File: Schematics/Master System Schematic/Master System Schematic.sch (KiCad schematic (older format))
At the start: 35 parts, among them J1 GND, J2 TS+, J3 TS-, SW1 GLVMS, SW10 SMD, SW11 BRAKE_SWITCH, SW12 SW_SPST_Pressure, SW13 SW_SPST_Pressure, SW2 SideMounted (BRB), SW3 SideMounted (BRB), SW4 Brake Over-Travel Switch, SW5 Latching Circuit Reset [Momen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, SW6 Cockpit Shutdown (BRB), SW7 TSMS, SW8 SMD, SW9 HVD, U3 FuseBox_PSZACCEPS052H, U4 Bender_Isometer_IR155-3204, U6 RinehartPM100DX_MotorControll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, U7 Emrax228HV_Motor

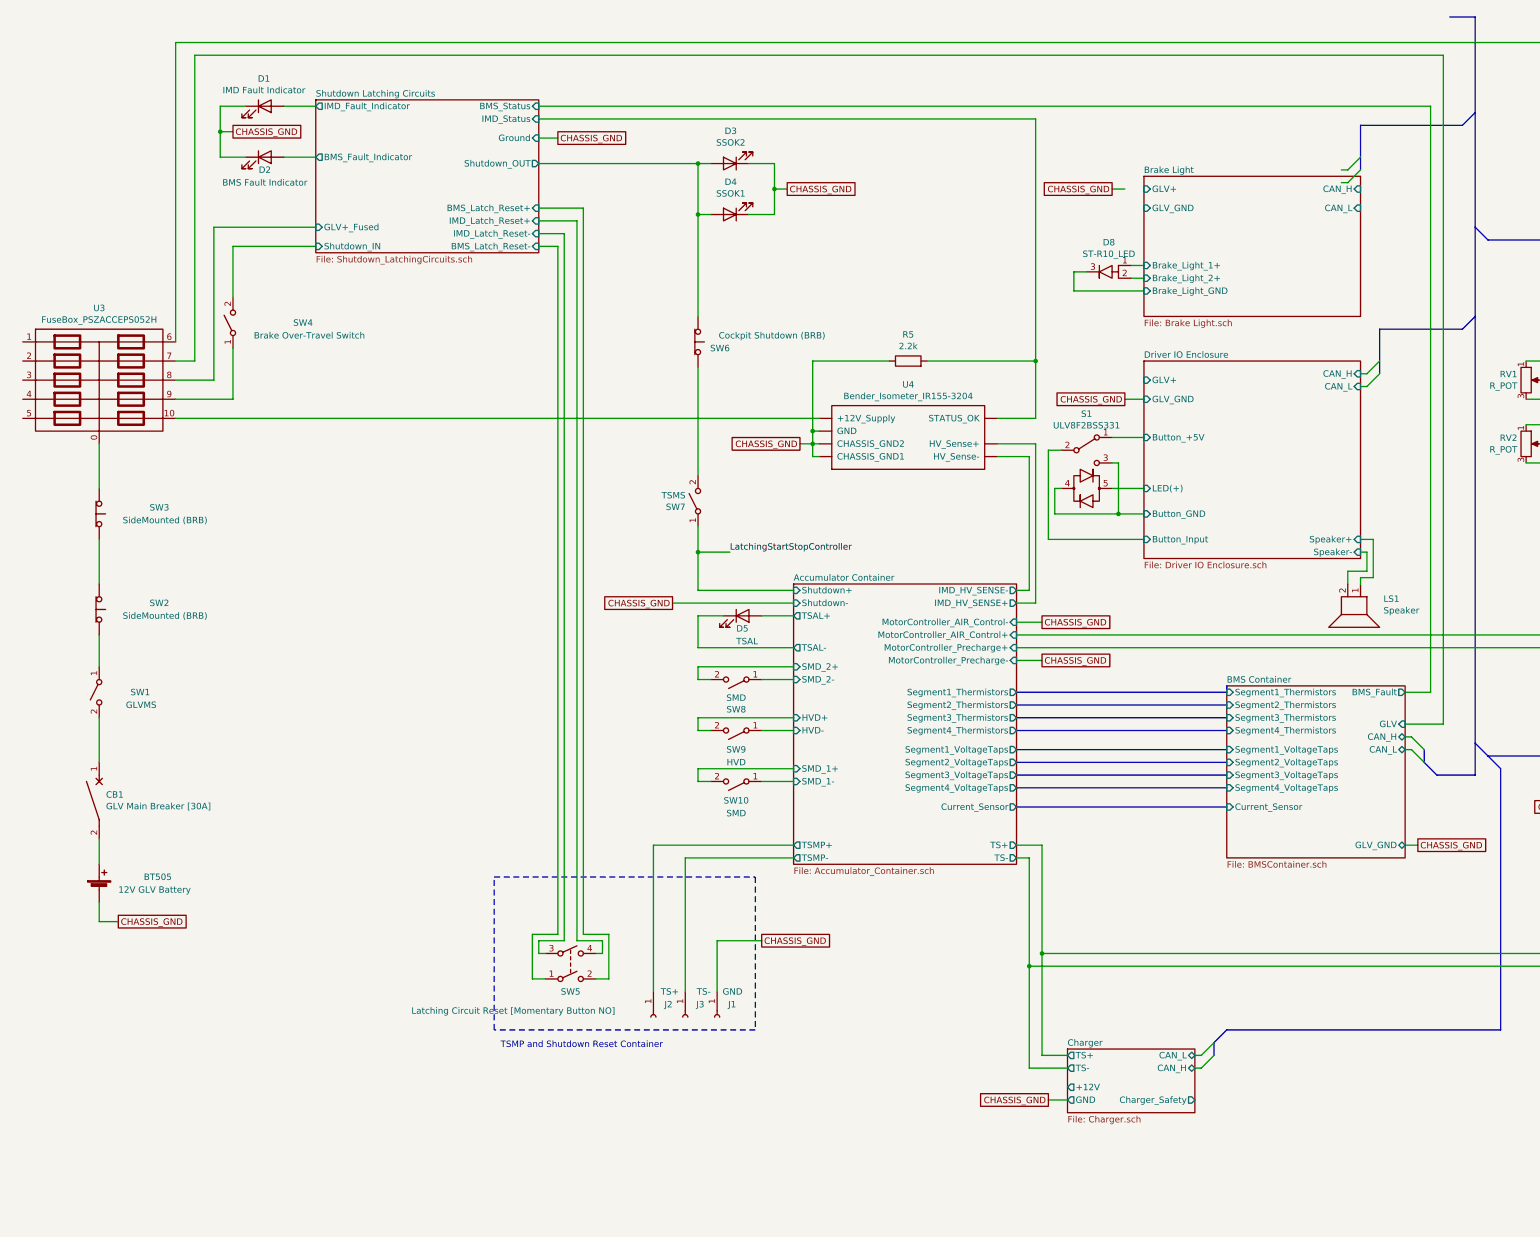
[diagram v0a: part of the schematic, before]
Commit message: Cooling Pump, TSMP container Updates
>Added Cooling pump relay
>Added Cooling pump
>Added +12V plug to TSMP container
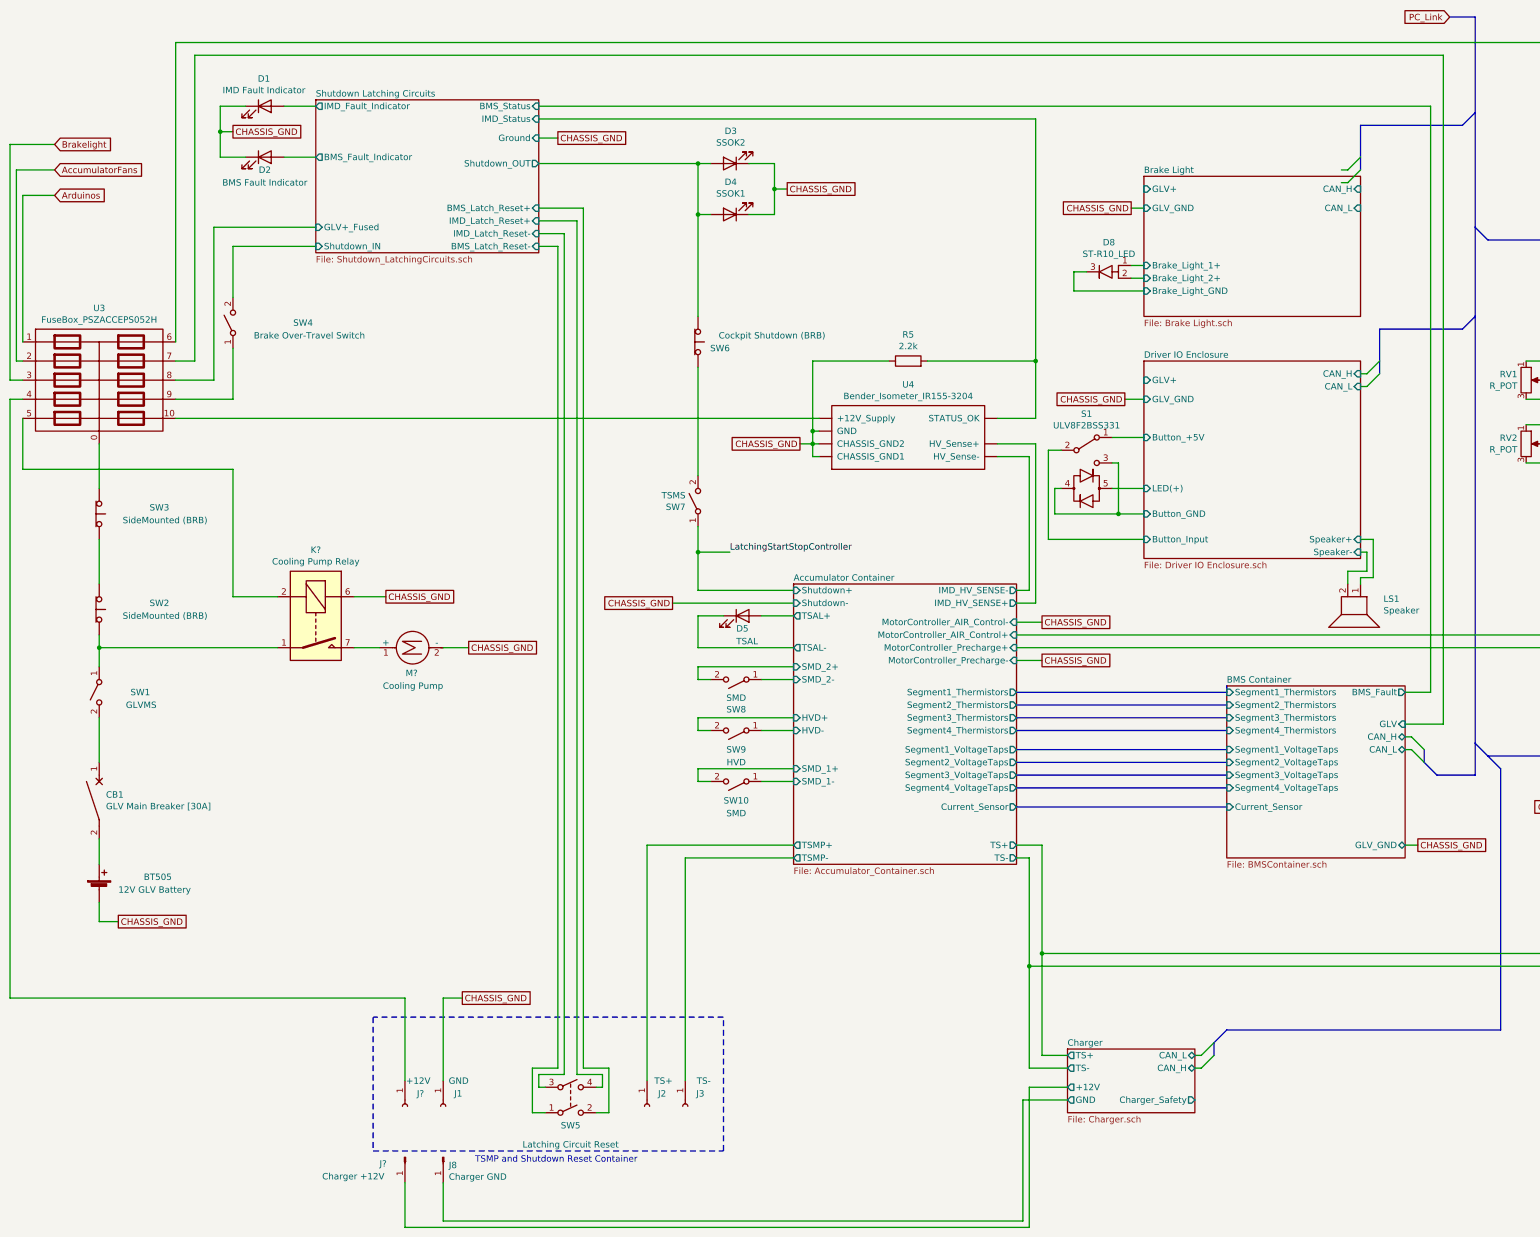
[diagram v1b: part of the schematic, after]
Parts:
- added J8: Charger GND, symbol Connector:Conn_01x01_Male
- added J?: Charger +12V, symbol Connector:Conn_01x01_Male
- added J?: +12V, symbol Connector:Conn_01x01_Female
- added K?: Cooling Pump Relay, Relay_THT:Relay_StandexMeder_DIP_LowProfile, symbol Master-System-Schematic-cache:Relay_DIPxx-1Axx-11x
- added M?: Cooling Pump, symbol Motor:Motor_DC
- SW5: value Latching Circuit Reset [Momentary Button NO] -> Latching Circuit Reset
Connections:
- net CHASSIS_GND: now also K?.6, M?.2 (-)
- net Charger/+12V: now also J?.1 (Pin_1)
- net at SW1.1 (A), SW2.2 (B): now also K?.1, K?.14
- net Arduinos: now reaches U3.1
- net AccumulatorFans: now reaches U3.2
- net Brakelight: now reaches U3.3
- net at U3.4: now also J?.1 (Pin_1)
- net at U3.5: now also K?.2
- new net: U3.6, U6.23 (CANB_H), U6.8 (Reverse_Enable_Switch)
- new net: U6.~ (TS-), U7.~ (AC3) (x2)
- new net: K?.7, K?.8, M?.1 (+)
- new net Charger/GND: J8.1 (Pin_1)
- now unconnected: U6.23 (CANB_H), U6.8 (Reverse_Enable_Switch)
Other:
- moved on the sheet: J1, J2, J3, SW5
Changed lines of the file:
@@
 EESchema Schematic File Version 4
-LIBS:Master System Schematic-cache
 EELAYER 30 0
 EELAYER END
@@
 	1250 6300 1250 6650
 Wire Wire Line
-	1250 5650 1250 5900
+	1250 5650 1250 5750
 Wire Wire Line
 	1250 4900 1250 5250
@@
 L Connector:Conn_01x01_Female J3
 U 1 1 5FB0713A
-P 5850 8650
-F 0 "J3" V 5750 8500 50  0000 L CNN
-F 1 "TS-" V 5650 8450 50  0000 L CNN
-F 2 "" H 5850 8650 50  0001 C CNN
-F 3 "~" H 5850 8650 50  0001 C CNN
-	1    5850 8650
+P 5850 9350
+F 0 "J3" V 5750 9200 50  0000 L CNN
+F 1 "TS-" V 5650 9150 50  0000 L CNN
+F 2 "" H 5850 9350 50  0001 C CNN
+F 3 "~" H 5850 9350 50  0001 C CNN
+	1    5850 9350
 	0    -1   1    0
 $EndComp
@@
 L Connector:Conn_01x01_Female J2
 U 1 1 5FB022E4
-P 5600 8650
-F 0 "J2" V 5500 8500 50  0000 L CNN
-F 1 "TS+" V 5400 8450 50  0000 L CNN
-F 2 "" H 5600 8650 50  0001 C CNN
-F 3 "~" H 5600 8650 50  0001 C CNN
-	1    5600 8650
+P 5550 9350
+F 0 "J2" V 5450 9200 50  0000 L CNN
+F 1 "TS+" V 5350 9150 50  0000 L CNN
+F 2 "" H 5550 9350 50  0001 C CNN
+F 3 "~" H 5550 9350 50  0001 C CNN
+	1    5550 9350
 	0    -1   1    0
 $EndComp
@@
 L Connector:Conn_01x01_Female J1
 U 1 1 5FAE402D
-P 6100 8650
-F 0 "J1" V 6000 8500 50  0000 L CNN
-F 1 "GND" V 5900 8450 50  0000 L CNN
-F 2 "" H 6100 8650 50  0001 C CNN
-F 3 "~" H 6100 8650 50  0001 C CNN
-	1    6100 8650
+P 3950 9350
+F 0 "J1" V 3850 9200 50  0000 L CNN
+F 1 "GND" V 3750 9150 50  0000 L CNN
+F 2 "" H 3950 9350 50  0001 C CNN
+F 3 "~" H 3950 9350 50  0001 C CNN
+	1    3950 9350
 	0    -1   1    0
 $EndComp
-Text Notes 4400 8900 0    50   ~ 0
+Text Notes 4200 9800 0    50   ~ 0
 TSMP and Shutdown Reset Container
 Text GLabel 5750 5400 0    50   UnSpc ~ 0
@@
 F15 "CAN_L" B R 11500 6550 50
 $EndSheet
-Text GLabel 6450 8050 2    50   UnSpc ~ 0
+Text GLabel 4100 8500 2    50   UnSpc ~ 0
 CHASSIS_GND
 $Comp
@@
 Wire Wire Line
 	5950 4400 5950 3550
-Wire Notes Line
-	4350 8750 4350 7550
-Wire Notes Line
-	4350 7550 6400 7550
-Wire Notes Line
-	6400 7550 6400 8750
-Wire Notes Line
-	6400 8750 4350 8750
 Wire Wire Line
 	11500 6100 11700 6100
@@
 	4850 1750 4700 1750
 Wire Wire Line
-	4750 8150 4700 8150
-Wire Wire Line
-	4700 8150 4700 8050
-Wire Wire Line
-	4700 8050 4900 8050
-Wire Wire Line
-	5150 8150 5200 8150
-Wire Wire Line
-	5200 8150 5200 8050
-Wire Wire Line
-	5200 8050 5000 8050
-Wire Wire Line
-	5150 8350 5250 8350
-Wire Wire Line
-	5250 8350 5250 8000
-Wire Wire Line
-	5250 8000 5050 8000
-Wire Wire Line
-	4750 8350 4650 8350
-Wire Wire Line
-	4650 8350 4650 8000
-Wire Wire Line
-	4650 8000 4850 8000
-Wire Wire Line
-	4850 2600 4850 8000
-Wire Wire Line
 	5050 2300 4700 2300
 Wire Wire Line
 	4700 2600 4850 2600
 Wire Wire Line
-	5050 2300 5050 8000
-Wire Wire Line
 	4700 2400 5000 2400
 Wire Wire Line
-	5000 2400 5000 8050
-Wire Wire Line
 	4900 2500 4700 2500
 Wire Wire Line
-	4900 2500 4900 8050
-Wire Wire Line
-	6700 7300 5600 7300
-Wire Wire Line
 	5850 7400 6700 7400
-Wire Wire Line
-	6450 8050 6100 8050
-Wire Wire Line
-	6100 8050 6100 8450
-$Comp
-L Switch:SW_DPST SW5
-U 1 1 5F864268
-P 4950 8250
-F 0 "SW5" H 4950 8050 50  0000 C CNN
-F 1 "Latching Circuit Reset [Momentary Button NO]" H 4500 7900 50  0000 C CNN
-F 2 "" H 4950 8250 50  0001 C CNN
-F 3 "~" H 4950 8250 50  0001 C CNN
-	1    4950 8250
-	1    0    0    -1
-$EndComp
 Wire Wire Line
 	1850 3950 6900 3950
@@
 F30 "Current_Sensor" O R 8450 7000 50
 $EndSheet
-Wire Wire Line
-	5600 7300 5600 8450
-Wire Wire Line
-	5850 7400 5850 8450
 Wire Bus Line
 	8450 7000 10100 7000
@@
 Wire Bus Line
 	11950 3250 11300 3250
-Wire Wire Line
-	8850 9300 8700 9300
-Text GLabel 8700 9300 0    50   UnSpc ~ 0
-CHASSIS_GND
 Entry Wire Line
 	10000 8950 9900 9050
@@
 Entry Bus Bus
 	12150 6600 12250 6700
-Text GLabel 9200 2150 0    50   UnSpc ~ 0
+Text GLabel 9350 2300 0    50   UnSpc ~ 0
 CHASSIS_GND
 Wire Wire Line
@@
 	9200 4100 9450 4100
 Wire Wire Line
-	9300 2150 9200 2150
+	9450 2300 9350 2300
 $Comp
 L NER:ST-R10_LED D8
@@
 Wire Wire Line
 	8900 2800 9000 2800
+$Comp
+L Connector:Conn_01x01_Male J8
+U 1 1 5F89DD3D
+P 3950 9750
+F 0 "J8" V 4012 9794 50  0000 L CNN
+F 1 "Charger GND" V 4103 9794 50  0000 L CNN
+F 2 "" H 3950 9750 50  0001 C CNN
+F 3 "~" H 3950 9750 50  0001 C CNN
+	1    3950 9750
+	0    1    1    0
+$EndComp
+$Comp
+L Connector:Conn_01x01_Male J?
+U 1 1 5F8D4529
+P 3650 9750
+F 0 "J?" V 3700 9550 50  0000 L CNN
+F 1 "Charger +12V" V 3800 9100 50  0000 L CNN
+F 2 "" H 3650 9750 50  0001 C CNN
+F 3 "~" H 3650 9750 50  0001 C CNN
+	1    3650 9750
+	0    1    1    0
+$EndComp
+$Comp
+L Connector:Conn_01x01_Female J?
+U 1 1 5F93092A
+P 3650 9350
+F 0 "J?" V 3550 9200 50  0000 L CNN
+F 1 "+12V" V 3450 9150 50  0000 L CNN
+F 2 "" H 3650 9350 50  0001 C CNN
+F 3 "~" H 3650 9350 50  0001 C CNN
+	1    3650 9350
+	0    -1   1    0
+$EndComp
+Wire Wire Line
+	5550 7300 6700 7300
+Connection ~ 1250 5750
+Wire Wire Line
+	1250 5750 1250 5900
+$Comp
+L Master-System-Schematic-cache:Relay_DIPxx-1Axx-11x K?
+U 1 1 5F9B5A7A
+P 2950 5550
+F 0 "K?" V 2383 5550 50  0000 C CNN
+F 1 "Cooling Pump Relay" V 2474 5550 50  0000 C CNN
+F 2 "Relay_THT:Relay_StandexMeder_DIP_LowProfile" H 3300 5500 50  0001 L CNN
+F 3 "" H 2950 5550 50  0001 C CNN
+	1    2950 5550
+	0    1    1    0
+$EndComp
+Wire Wire Line
+	1250 5750 2650 5750
+Wire Wire Line
+	650  3950 650  4350
+Wire Wire Line
+	2300 4350 2300 5350
+Wire Wire Line
+	2300 5350 2650 5350
+Wire Wire Line
+	3250 5350 3500 5350
+Text GLabel 3500 5350 2    50   UnSpc ~ 0
+CHASSIS_GND
+$Comp
+L Motor:Motor_DC M?
+U 1 1 5FA2966E
+P 3650 5750
+F 0 "M?" V 3450 5650 50  0000 L CNN
+F 1 "Cooling Pump" V 3350 5450 50  0000 L CNN
+F 2 "" H 3650 5660 50  0001 C CNN
+F 3 "~" H 3650 5660 50  0001 C CNN
+	1    3650 5750
+	0    -1   -1   0
+$EndComp
+Wire Wire Line
+	3250 5750 3450 5750
+Text GLabel 4150 5750 2    50   UnSpc ~ 0
+CHASSIS_GND
+Wire Wire Line
+	4150 5750 3950 5750
+Wire Wire Line
+	650  4350 2300 4350
+Wire Wire Line
+	650  3800 550  3800
+Wire Wire Line
+	550  3800 550  8500
+Wire Wire Line
+	650  3350 650  2200
+Wire Wire Line
+	650  2200 900  2200
+Text GLabel 900  2200 2    50   Input ~ 0
+Arduinos
+Wire Wire Line
+	650  3500 600  3500
+Wire Wire Line
+	600  3500 600  2000
+Wire Wire Line
+	600  2000 900  2000
+Text GLabel 900  2000 2    50   Input ~ 0
+AccumulatorFans
+Wire Wire Line
+	650  3650 550  3650
+Wire Wire Line
+	550  3650 550  1800
+Wire Wire Line
+	550  1800 900  1800
+Text GLabel 900  1800 2    50   Input ~ 0
+Brakelight
+$Comp
+L Switch:SW_DPST SW5
+U 1 1 5F864268
+P 4950 9300
+F 0 "SW5" H 4950 9100 50  0000 C CNN
+F 1 "Latching Circuit Reset" H 4950 8950 50  0000 C CNN
+F 2 "" H 4950 9300 50  0001 C CNN
+F 3 "~" H 4950 9300 50  0001 C CNN
+	1    4950 9300
+	1    0    0    -1
+$EndComp
+Wire Wire Line
+	4650 9050 4850 9050
+Wire Wire Line
+	4650 9400 4650 9050
+Wire Wire Line
+	4750 9400 4650 9400
+Wire Wire Line
+	5250 9050 5050 9050
+Wire Wire Line
+	5250 9400 5250 9050
+Wire Wire Line
+	5150 9400 5250 9400
+Wire Wire Line
+	5200 9100 5000 9100
+Wire Wire Line
+	5200 9200 5200 9100
+Wire Wire Line
+	5150 9200 5200 9200
+Wire Wire Line
+	4700 9100 4900 9100
+Wire Wire Line
+	4700 9200 4700 9100
+Wire Wire Line
+	4750 9200 4700 9200
+Wire Wire Line
+	5850 7400 5850 9150
+Wire Wire Line
+	5550 7300 5550 9150
+Wire Wire Line
+	3950 8500 4100 8500
+Wire Wire Line
+	3650 8500 550  8500
+Wire Wire Line
+	3650 8500 3650 9150
+Wire Wire Line
+	3950 8500 3950 9150
+Wire Wire Line
+	3650 9950 3650 10300
+Wire Wire Line
+	3650 10300 8550 10300
+Wire Wire Line
+	8550 10300 8550 9200
+Wire Wire Line
+	8550 9200 8850 9200
+Wire Wire Line
+	3950 9950 3950 10250
+Wire Wire Line
+	3950 10250 8500 10250
+Wire Wire Line
+	8500 10250 8500 9300
+Wire Wire Line
+	8500 9300 8850 9300
+Wire Notes Line
+	6150 9700 6150 8650
+Wire Notes Line
+	6150 8650 3400 8650
+Wire Notes Line
+	3400 8650 3400 9700
+Wire Notes Line
+	3400 9700 6150 9700
+Wire Wire Line
+	4850 2600 4850 9050
+Wire Wire Line
+	4900 2500 4900 9100
+Wire Wire Line
+	5000 2400 5000 9100
+Wire Wire Line
+	5050 2300 5050 9050
+Text GLabel 11850 800  0    50   Input ~ 0
+PC_Link
+Wire Bus Line
+	11300 3250 11300 3600
 Wire Bus Line
 	14550 2550 14550 3150
@@
 	11150 1650 11150 2000
 Wire Bus Line
-	11300 3250 11300 3600
-Wire Bus Line
 	12050 800  12050 6750

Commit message: Added anotations
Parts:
- gave numbers to parts that had none: 4
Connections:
- new net: U3.6, U6.23 (CANB_H), U6.8 (Reverse_Enable_Switch)
- new net: U6.~ (TS-), U7.~ (AC3) (x2)
- now unconnected: U6.23 (CANB_H), U6.8 (Reverse_Enable_Switch)
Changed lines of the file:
@@
 $EndComp
 $Comp
-L Connector:Conn_01x01_Male J?
+L Connector:Conn_01x01_Male J11
 U 1 1 5F8D4529
 P 3650 9750
-F 0 "J?" V 3700 9550 50  0000 L CNN
+F 0 "J11" V 3700 9550 50  0000 L CNN
 F 1 "Charger +12V" V 3800 9100 50  0000 L CNN
 F 2 "" H 3650 9750 50  0001 C CNN
@@
 $EndComp
 $Comp
-L Connector:Conn_01x01_Female J?
+L Connector:Conn_01x01_Female J10
 U 1 1 5F93092A
 P 3650 9350
-F 0 "J?" V 3550 9200 50  0000 L CNN
+F 0 "J10" V 3550 9200 50  0000 L CNN
 F 1 "+12V" V 3450 9150 50  0000 L CNN
 F 2 "" H 3650 9350 50  0001 C CNN
@@
 	1250 5750 1250 5900
 $Comp
-L Master-System-Schematic-cache:Relay_DIPxx-1Axx-11x K?
+L Master-System-Schematic-cache:Relay_DIPxx-1Axx-11x K12
 U 1 1 5F9B5A7A
 P 2950 5550
-F 0 "K?" V 2383 5550 50  0000 C CNN
+F 0 "K12" V 2383 5550 50  0000 C CNN
 F 1 "Cooling Pump Relay" V 2474 5550 50  0000 C CNN
 F 2 "Relay_THT:Relay_StandexMeder_DIP_LowProfile" H 3300 5500 50  0001 L CNN
@@
 CHASSIS_GND
 $Comp
-L Motor:Motor_DC M?
+L Motor:Motor_DC M1
 U 1 1 5FA2966E
 P 3650 5750
-F 0 "M?" V 3450 5650 50  0000 L CNN
+F 0 "M1" V 3450 5650 50  0000 L CNN
 F 1 "Cooling Pump" V 3350 5450 50  0000 L CNN
 F 2 "" H 3650 5660 50  0001 C CNN

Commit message: Wire Runs and cleanup
>Cleaned up some wire runs
>Added Charger safety connection
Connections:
- net Arduinos is gone; now on net AccumulatorFans: U3.1
- net AccumulatorFans: no longer U3.2
- net Brake Light/GLV+: now also U3.2
- net Brakelight: no longer names the net of U3.3
- new net: U3.6, U6.23 (CANB_H), U6.8 (Reverse_Enable_Switch)
- new net: U6.~ (TS-), U7.~ (AC3) (x2)
- now unconnected: U6.23 (CANB_H), U6.8 (Reverse_Enable_Switch)
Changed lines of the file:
@@
 	0    -1   1    0
 $EndComp
-Text Notes 4200 9800 0    50   ~ 0
+Text Notes 4750 9800 0    50   ~ 0
 TSMP and Shutdown Reset Container
 Text GLabel 5750 5400 0    50   UnSpc ~ 0
 CHASSIS_GND
 $Sheet
-S 8850 8900 1000 500
+S 8700 8900 1000 500
 U 61ECC7CF
 F0 "Charger" 50
 F1 "Charger.sch" 50
-F2 "+12V" O L 8850 9200 50
-F3 "TS+" O L 8850 8950 50
-F4 "TS-" O L 8850 9050 50
-F5 "Charger_Safety" O R 9850 9300 50
-F6 "CAN_L" B R 9850 8950 50
-F7 "CAN_H" B R 9850 9050 50
-F8 "GND" O L 8850 9300 50
+F2 "+12V" O L 8700 9200 50
+F3 "TS+" O L 8700 8950 50
+F4 "TS-" O L 8700 9050 50
+F5 "Charger_Safety" O R 9700 9300 50
+F6 "CAN_L" B R 9700 8950 50
+F7 "CAN_H" B R 9700 9050 50
+F8 "GND" O L 8700 9300 50
 $EndSheet
 Text GLabel 8650 5850 2    50   UnSpc ~ 0
@@
 F14 "CAN_H" B R 11500 6450 50
 F15 "CAN_L" B R 11500 6550 50
+F16 "ChargeSafety" O L 10100 7300 50
 $EndSheet
 Text GLabel 4100 8500 2    50   UnSpc ~ 0
@@
 Wire Wire Line
 	11500 6100 11700 6100
-Wire Wire Line
-	8650 8950 8850 8950
-Wire Wire Line
-	8550 9050 8850 9050
 Wire Wire Line
 	11700 6100 11700 1500
@@
 Text GLabel 8650 5550 2    50   UnSpc ~ 0
 CHASSIS_GND
-Wire Wire Line
-	8450 5650 15400 5650
-Wire Wire Line
-	15400 5650 15400 7950
-Wire Wire Line
-	15400 7950 15200 7950
 $Comp
 L Switch:SW_SPST SW?
@@
 	11950 3250 11300 3250
 Entry Wire Line
-	10000 8950 9900 9050
-Entry Wire Line
-	10000 8850 9900 8950
-Wire Bus Line
-	10000 8950 10000 8850
+	9850 8950 9750 9050
+Entry Wire Line
+	9850 8850 9750 8950
+Wire Bus Line
+	9850 8950 9850 8850
 Entry Bus Bus
-	10100 8750 10000 8850
-Wire Wire Line
-	9900 8950 9850 8950
-Wire Wire Line
-	9850 9050 9900 9050
+	9950 8750 9850 8850
+Wire Wire Line
+	9750 8950 9700 8950
+Wire Wire Line
+	9700 9050 9750 9050
 Wire Bus Line
 	12250 8750 12250 6700
-Wire Bus Line
-	10100 8750 12250 8750
 Entry Bus Bus
 	12150 6600 12250 6700
@@
 Wire Wire Line
 	650  2200 900  2200
-Text GLabel 900  2200 2    50   Input ~ 0
-Arduinos
-Wire Wire Line
-	650  3500 600  3500
-Wire Wire Line
-	600  3500 600  2000
-Wire Wire Line
-	600  2000 900  2000
-Text GLabel 900  2000 2    50   Input ~ 0
-AccumulatorFans
-Wire Wire Line
-	650  3650 550  3650
-Wire Wire Line
-	550  3650 550  1800
-Wire Wire Line
-	550  1800 900  1800
-Text GLabel 900  1800 2    50   Input ~ 0
-Brakelight
 $Comp
 L Switch:SW_DPST SW5
@@
 	8550 10300 8550 9200
 Wire Wire Line
-	8550 9200 8850 9200
-Wire Wire Line
 	3950 9950 3950 10250
 Wire Wire Line
@@
 Wire Wire Line
 	8500 10250 8500 9300
-Wire Wire Line
-	8500 9300 8850 9300
 Wire Notes Line
 	6150 9700 6150 8650
@@
 Text GLabel 11850 800  0    50   Input ~ 0
 PC_Link
+Wire Wire Line
+	600  750  9050 750
+Wire Bus Line
+	9450 3650 8750 3650
+Wire Bus Line
+	8750 3650 8750 700
+Connection ~ 8750 700
+Wire Bus Line
+	12950 3150 12750 3150
+Wire Bus Line
+	12750 3150 12750 700
+Wire Bus Line
+	8750 700  12750 700
+Wire Bus Line
+	550  3650 650  3650
+Wire Bus Line
+	550  700  550  3650
+Wire Bus Line
+	550  700  8750 700
+Wire Wire Line
+	650  3500 600  3500
+Wire Wire Line
+	600  3500 600  750
+Wire Wire Line
+	9050 2150 9050 750
+Wire Wire Line
+	9050 2150 9450 2150
+Wire Wire Line
+	8450 5650 15450 5650
+Text Label 900  2200 0    50   ~ 0
+AccumulatorFans
+Text Label 15450 5650 0    50   ~ 0
+MotorControllerAIRControl
+Wire Wire Line
+	8500 9300 8700 9300
+Wire Wire Line
+	8550 9050 8700 9050
+Wire Wire Line
+	8550 9200 8700 9200
+Wire Wire Line
+	8650 8950 8700 8950
+Wire Bus Line
+	9950 8750 12250 8750
+Wire Wire Line
+	9700 9300 10000 9300
+Wire Wire Line
+	10000 9300 10000 7300
+Wire Wire Line
+	10000 7300 10100 7300
 Wire Bus Line
 	11300 3250 11300 3600
